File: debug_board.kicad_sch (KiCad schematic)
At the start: 0 parts

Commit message: linked everything together. still need to add capacitors
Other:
- sheet STM32 ports: added CANH, CANL, I2C_SCL, I2C_SDA, USB+, USB-; removed none
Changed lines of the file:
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@@
+	(wire
+		(pts
+			(xy 125.73 104.14) (xy 125.73 101.6)
+		)
+		(stroke
+			(width 0)
+			(type default)
+		)
+	)
+	(wire
+		(pts
+			(xy 134.62 113.03) (xy 134.62 101.6)
+		)
+		(stroke
+			(width 0)
+			(type default)
+		)
+	)
+	(wire
+		(pts
+			(xy 96.52 93.98) (xy 96.52 99.06)
+		)
+		(stroke
+			(width 0)
+			(type default)
+		)
+	)
 	(wire
 		(pts
@@
 	(wire
 		(pts
+			(xy 114.3 104.14) (xy 125.73 104.14)
+		)
+		(stroke
+			(width 0)
+			(type default)
+		)
+	)
+	(wire
+		(pts
 			(xy 114.3 54.61) (xy 121.92 54.61)
 		)
@@
 	(wire
 		(pts
+			(xy 137.16 115.57) (xy 114.3 115.57)
+		)
+		(stroke
+			(width 0)
+			(type default)
+		)
+	)
+	(wire
+		(pts
 			(xy 114.3 41.91) (xy 121.92 41.91)
 		)
@@
 	(wire
 		(pts
+			(xy 114.3 113.03) (xy 134.62 113.03)
+		)
+		(stroke
+			(width 0)
+			(type default)
+		)
+	)
+	(wire
+		(pts
+			(xy 137.16 101.6) (xy 137.16 115.57)
+		)
+		(stroke
+			(width 0)
+			(type default)
+		)
+	)
+	(wire
+		(pts
+			(xy 93.98 93.98) (xy 93.98 99.06)
+		)
+		(stroke
+			(width 0)
+			(type default)
+		)
+	)
+	(wire
+		(pts
 			(xy 114.3 52.07) (xy 121.92 52.07)
 		)
@@
 	(wire
 		(pts
+			(xy 128.27 106.68) (xy 128.27 101.6)
+		)
+		(stroke
+			(width 0)
+			(type default)
+		)
+	)
+	(wire
+		(pts
 			(xy 82.55 78.74) (xy 88.9 78.74)
 		)
@@
 		)
 	)
+	(wire
+		(pts
+			(xy 114.3 106.68) (xy 128.27 106.68)
+		)
+		(stroke
+			(width 0)
+			(type default)
+		)
+	)
 	(sheet
-		(at 60.96 50.8)
-		(size 21.59 11.43)
-		(fields_autoplaced yes)
+		(at 88.9 99.06)
+		(size 25.4 19.05)
 		(stroke
 			(width 0.1524)
@@
 		)
 		(property "Sheetname" "STM32"
-			(at 60.96 50.0884 0)
+			(at 88.646 120.142 0)
 			(effects
 				(font
@@
 		)
 		(property "Sheetfile" "STM32.kicad_sch"
-			(at 60.96 62.8146 0)
+			(at 88.9 118.6946 0)
 			(effects
 				(font
@@
 				)
 				(justify left top)
+				(hide yes)
+			)
+		)
+		(pin "I2C_SCL" input
+			(at 114.3 104.14 0)
+			(effects
+				(font
+					(size 1.27 1.27)
+				)
+				(justify right)
+			)
+		)
+		(pin "USB+" input
+			(at 96.52 99.06 90)
+			(effects
+				(font
+					(size 1.27 1.27)
+				)
+				(justify right)
+			)
+		)
+		(pin "USB-" input
+			(at 93.98 99.06 90)
+			(effects
+				(font
+					(size 1.27 1.27)
+				)
+				(justify right)
+			)
+		)
+		(pin "I2C_SDA" input
+			(at 114.3 106.68 0)
+			(effects
+				(font
+					(size 1.27 1.27)
+				)
+				(justify right)
+			)
+		)
+		(pin "CANL" bidirectional
+			(at 114.3 115.57 0)
+			(effects
+				(font
+					(size 1.27 1.27)
+				)
+				(justify right)
+			)
+		)
+		(pin "CANH" bidirectional
+			(at 114.3 113.03 0)
+			(effects
+				(font
+					(size 1.27 1.27)
+				)
+				(justify right)
 			)
 		)
@@
 	(sheet
 		(at 121.92 39.37)
-		(size 19.05 67.31)
+		(size 19.05 62.23)
 		(fields_autoplaced yes)
 		(stroke
@@
 		)
 		(property "Sheetfile" "connector.kicad_sch"
-			(at 121.92 107.2646 0)
+			(at 121.92 102.1846 0)
 			(effects
 				(font
@@
 		)
 		(pin "CANH" input
-			(at 134.62 106.68 270)
+			(at 134.62 101.6 270)
 			(effects
 				(font
@@
 		)
 		(pin "CANL" input
-			(at 137.16 106.68 270)
+			(at 137.16 101.6 270)
 			(effects
 				(font
@@
 		)
 		(pin "I2C_SCL" input
-			(at 125.73 106.68 270)
+			(at 125.73 101.6 270)
 			(effects
 				(font
@@
 		)
 		(pin "I2C_SDA" input
-			(at 128.27 106.68 270)
-			(effects
-				(font
+			(at 128.27 101.6 270)
+			(effects
+				(font

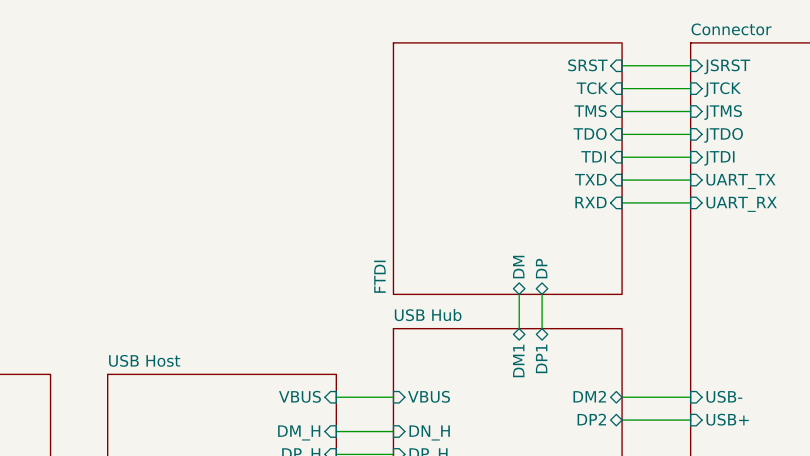
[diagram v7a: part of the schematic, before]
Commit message: started pcb layout, host and usbhub done
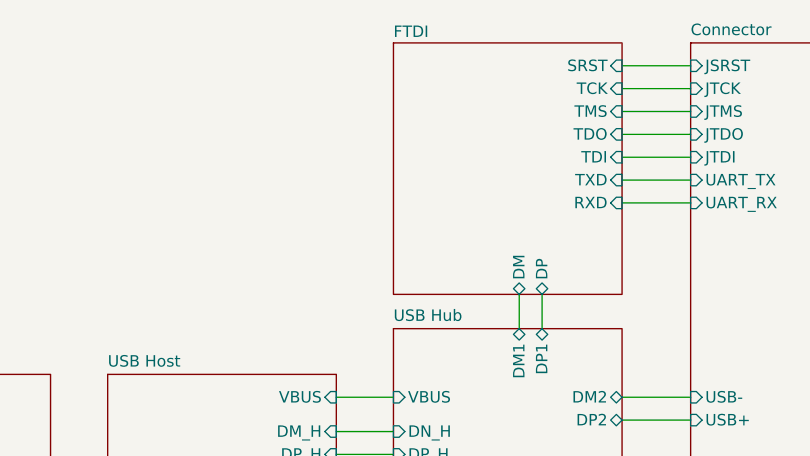
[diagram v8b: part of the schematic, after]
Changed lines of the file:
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@@
 		(at 88.9 39.37)
 		(size 25.4 27.94)
-		(fields_autoplaced yes)
 		(stroke
 			(width 0.1524)
@@
 		)
 		(property "Sheetname" "FTDI"
-			(at 88.1884 67.31 90)
+			(at 88.9 38.862 0)
 			(effects
 				(font
